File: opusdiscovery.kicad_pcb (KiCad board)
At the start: 2 copper layers, 99.1 x 99.1 mm, 57 parts, among them IC1 WD1772, IC11 GAL22V10, IC12 L7805, IC2 AT28C256, IC3 6264, IC4 GAL22V10, IC5 74LS06, IC9 74LS00, J1 ZX_Spectrum_Connector_GENERIC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, J2 Conn_02x17_Odd_Even, J3 Conn_02x13_Odd_Even, J4 DB9_Male, SW2 SW_DPST_x2, SW3 SW_DIP_x03, U1 74LS73, U10 74LS38, U2 74LS139, U3 6821, Y1 8.000Mhz

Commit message: typos
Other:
- board text added: "NOR = INV ||"
- board text removed: "NOR || INV ="
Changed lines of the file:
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@@
       (rotate (xyz 0 0 90))
     )
+    (model ${KISYS3DMOD}/Button_Switch_THT.3dshapes/SW_DIP_x2_W7.62mm_Slide.step
+      (at (xyz 0 0 0))
+      (scale (xyz 1 1 1))
+      (rotate (xyz 0 0 0))
+    )
   )
   (module Housings_DIP:DIP-14_W7.62mm_LongPads (layer F.Cu)
@@
     (pad 1 thru_hole circle (at 0 0 180) (size 1.6 1.6) (drill 0.8) (layers *.Cu *.Mask)
       (net 1 GND))
-    (model ${KISYS3DMOD}/Capacitors_THT.3dshapes/C_Disc_D5.0mm_W2.5mm_P5.00mm.wrl
+    (model ${KISYS3DMOD}/Capacitor_THT.3dshapes/C_Disc_D5.0mm_W2.5mm_P5.00mm.wrl
       (at (xyz 0 0 0))
       (scale (xyz 1 1 1))
@@
     (effects (font (size 1 1) (thickness 0.2)))
   )
-  (gr_text "NOR ||\nINV  =" (at 115.697 22.86) (layer F.SilkS)
+  (gr_text "NOR = \nINV  ||" (at 113.665 33.02 90) (layer F.SilkS)
     (effects (font (size 0.75 0.75) (thickness 0.15)) (justify left))
   )
-  (gr_text "1-2,3-4 AT\n2-3   SH" (at 81.534 23.241) (layer F.SilkS)
+  (gr_text "1-2,3-4 AT\n2-3   SH" (at 78.74 38.1 90) (layer F.SilkS)
     (effects (font (size 0.75 0.75) (thickness 0.15)) (justify right))
   )
@@
   (gr_line (start 97.79 132.08) (end 98.552 131.572) (layer F.SilkS) (width 0.25))
   (gr_arc (start 97.790001 133.35) (end 98.806 132.588) (angle -106.3) (layer F.SilkS) (width 0.25))
-  (gr_arc (start 139.954529 133.349293) (end 140.970528 132.587293) (angle -106.3) (layer F.SilkS) (width 0.25))
-  (gr_arc (start 137.16 133.35) (end 138.175999 132.588) (angle -106.3) (layer F.SilkS) (width 0.25))
-  (gr_line (start 140.716 131.572) (end 141.986 131.572) (layer F.SilkS) (width 0.25))
-  (gr_line (start 139.954 132.08) (end 140.716 131.572) (layer F.SilkS) (width 0.25))
-  (gr_line (start 136.652 131.572) (end 137.16 132.08) (layer F.SilkS) (width 0.25))
-  (gr_line (start 134.366 131.572) (end 136.652 131.572) (layer F.SilkS) (width 0.25))
-  (gr_text "(2-3) +2A/+3          48K/128K (1-2)  " (at 140.208 131.826) (layer F.SilkS)
+  (gr_arc (start 141.859529 133.349293) (end 142.875528 132.587293) (angle -106.3) (layer F.SilkS) (width 0.25))
+  (gr_arc (start 139.065 133.35) (end 140.080999 132.588) (angle -106.3) (layer F.SilkS) (width 0.25))
+  (gr_line (start 142.621 131.572) (end 143.891 131.572) (layer F.SilkS) (width 0.25))
+  (gr_line (start 141.859 132.08) (end 142.621 131.572) (layer F.SilkS) (width 0.25))
+  (gr_line (start 138.557 131.572) (end 139.065 132.08) (layer F.SilkS) (width 0.25))
+  (gr_line (start 136.271 131.572) (end 138.557 131.572) (layer F.SilkS) (width 0.25))
+  (gr_text "(2-3) +2A/+3          48K/128K (1-2)  " (at 142.113 131.826) (layer F.SilkS)
     (effects (font (size 1.25 1.25) (thickness 0.25)))
   )
-  (gr_text 3 (at 135.89 133.858) (layer F.SilkS)
+  (gr_text 3 (at 137.795 133.858) (layer F.SilkS)
     (effects (font (size 1 1) (thickness 0.2)))
   )
-  (gr_text 2 (at 138.43 133.858) (layer F.SilkS)
+  (gr_text 2 (at 140.335 133.858) (layer F.SilkS)
     (effects (font (size 1 1) (thickness 0.2)))
   )
@@
     (effects (font (size 1 1) (thickness 0.2)) (justify mirror))
   )
-  (gr_text 1 (at 73.025 23.114) (layer F.SilkS)
+  (gr_text 1 (at 73.66 38.1) (layer F.SilkS)
     (effects (font (size 1 1) (thickness 0.2)))
   )
@@
     (effects (font (size 1.5 1.5) (thickness 0.3)))
   )
-  (gr_text 1 (at 141.224 133.858) (layer F.SilkS)
+  (gr_text 1 (at 143.129 133.858) (layer F.SilkS)
     (effects (font (size 1 1) (thickness 0.2)))
   )

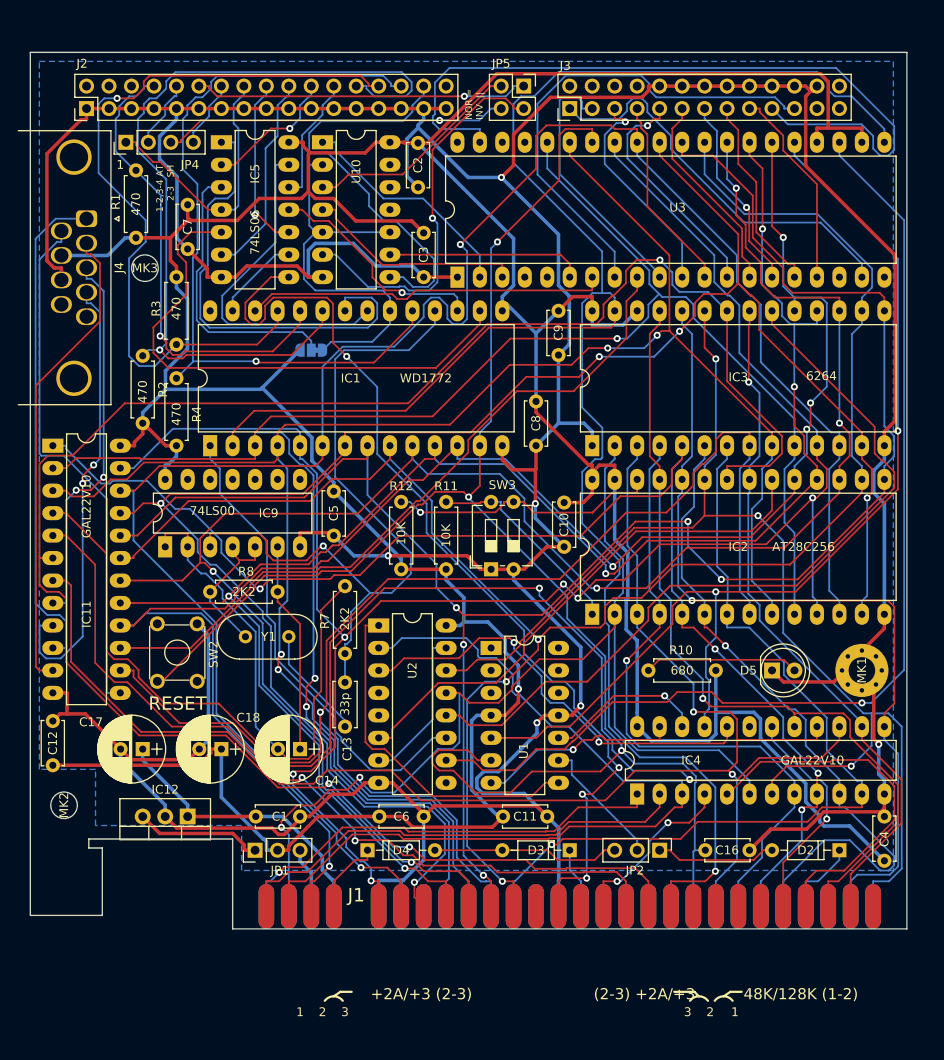
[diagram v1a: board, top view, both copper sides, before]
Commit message: upgrade to kicad 6 and include roms directory
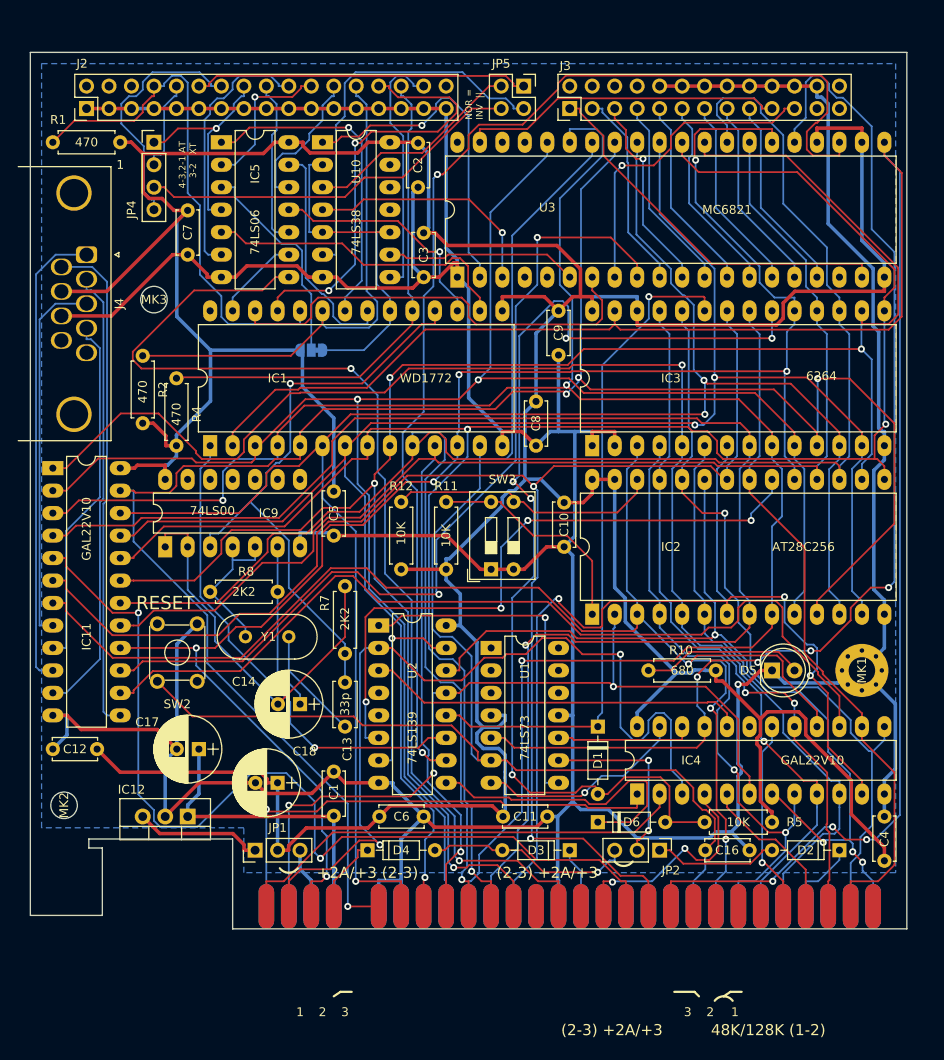
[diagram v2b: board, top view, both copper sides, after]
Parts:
- removed R3: 470, Resistors_THT:R_Axial_DIN0207_L6.3mm_D2.5mm_P7.62mm_Horizontal
- added D1: 1N4148, Diode_THT:D_DO-35_SOD27_P7.62mm_Horizontal, F.Cu at (127.6, 101.6)
- added D6: 1N4148, Diode_THT:D_DO-35_SOD27_P7.62mm_Horizontal, F.Cu at (127.6, 112.4)
- added R5: 10K, Resistor_THT:R_Axial_DIN0207_L6.3mm_D2.5mm_P7.62mm_Horizontal, F.Cu at (139.7, 112.4)
- JP6: footprint Jumper:SolderJumper-3_P1.3mm_Bridged12_RoundedPad1.0x1.5mm -> SINCLAIR:SolderJumper-3_P1.3mm_Bridged12_RoundedPad1.0x1.5mm
- SW3: footprint Button_Switch_THT:SW_DIP_SPSTx02_Slide_6.7x6.64mm_W7.62mm_P2.54mm_LowProfile -> Button_Switch_THT:SW_DIP_SPSTx02_Slide_9.78x7.26mm_W7.62mm_P2.54mm
- U3: value 6821 -> MC6821
- moved R1 9.92 mm to (66.0, 35.6), turned to 0 degrees
- moved C18 7.41 mm to (91.4, 108.0)
- moved C1 6.35 mm to (97.8, 106.7), turned to -90 degrees
- moved C17 6.35 mm to (82.5, 104.1)
- moved C14 5.08 mm to (94.0, 99.1)
- moved J4 4.06 mm to (69.8, 48.3)
- moved MK3 3.70 mm to (77.5, 53.3)
- moved C12 3.17 mm to (66.0, 104.1), turned to 0 degrees
- moved JP4 3.17 mm to (77.5, 35.6), turned to 0 degrees
- moved IC11 2.54 mm to (66.0, 72.4)
- moved C7 0.63 mm to (81.3, 48.3)
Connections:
- net ZX_I_ROMOE renamed Net-(JP2-Pad2)
- IC3 pad 2: /A12 -> GND
- IC3 pad 23: /A11 -> RAM_CS1
- U2 pad 12: RAM_CS -> RAM_CS1
- U2 pad 9: (no net) -> RAM_CS2
- U3 pad 20: (no net) -> +5V
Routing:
- net RAM_CS1: track 0.00 -> 76.5 mm, vias 0 -> 1
- net /RD: track 224.4 -> 169.5 mm, vias 3 -> 2
- net Net-(J3-Pad19): track 86.8 -> 36.6 mm
- net Net-(IC1-Pad25): track 86.3 -> 49.2 mm, vias 1 -> 2
- net /A11: track 139.9 -> 103.4 mm, vias 3 -> 4
- net /TRACK_0: track 94.6 -> 59.0 mm, vias 1 -> 0
- net RAM_CS2: track 0.00 -> 33.9 mm
- net Net-(IC1-Pad19): track 87.5 -> 57.1 mm, vias 1 -> 0
- net RAM_CS: track 88.9 -> 119.0 mm, vias 0 -> 5
- net /A12: track 120.1 -> 92.3 mm, vias 2 -> 3
- net GND: track 577.0 -> 550.3 mm, vias 6 -> 1
- net Net-(IC1-Pad16): track 60.8 -> 35.7 mm
- net /RFSH: track 41.3 -> 17.5 mm
- net /RESET: track 189.5 -> 166.8 mm, vias 3 -> 0
- net JOY_EN: track 80.2 -> 100.9 mm, vias 0 -> 2
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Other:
- net class Default removed
- net class power removed
- board text added: "(2-3) +2A/+3"
- board text added: "(C) 2019-2021 PCB by A. ALEA"
- board text added: "4-3,2-1 AT 3-2 XT"
- board text removed: "(C) 2019 PCB by A. ALEA"
- board text removed: "1-2,3-4 AT 2-3 SH"
